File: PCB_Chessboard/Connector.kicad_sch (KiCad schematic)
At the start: 44 parts, among them J10 Conn_01x02, J11 Conn_01x02, J12 Conn_01x02, J13 Conn_01x02, J14 Conn_01x02, J15 Conn_01x02, J16 Conn_01x02, J17 Conn_01x02, J18 Conn_01x02, J19 Conn_01x03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

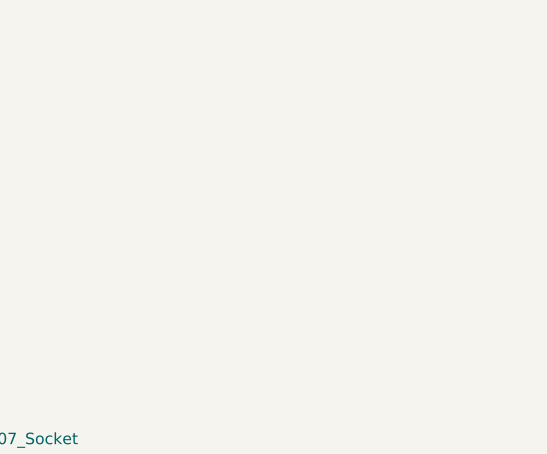
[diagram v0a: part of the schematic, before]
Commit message: PCB quadrant with mounting Hole
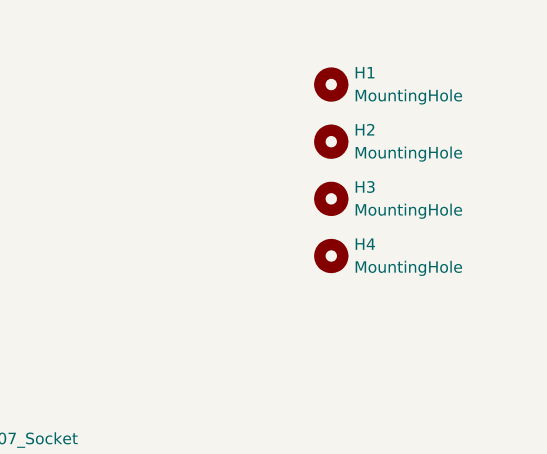
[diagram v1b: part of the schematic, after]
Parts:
- added H1, H2, H3, H4: MountingHole, MountingHole:MountingHole_4mm, symbol Mechanical:MountingHole
